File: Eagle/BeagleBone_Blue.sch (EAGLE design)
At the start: 129 parts, among them M1 JST_ZH_2, M2 JST_ZH_2, M3 JST_ZH_2, M4 JST_ZH_2, Q3 MOSFET-N

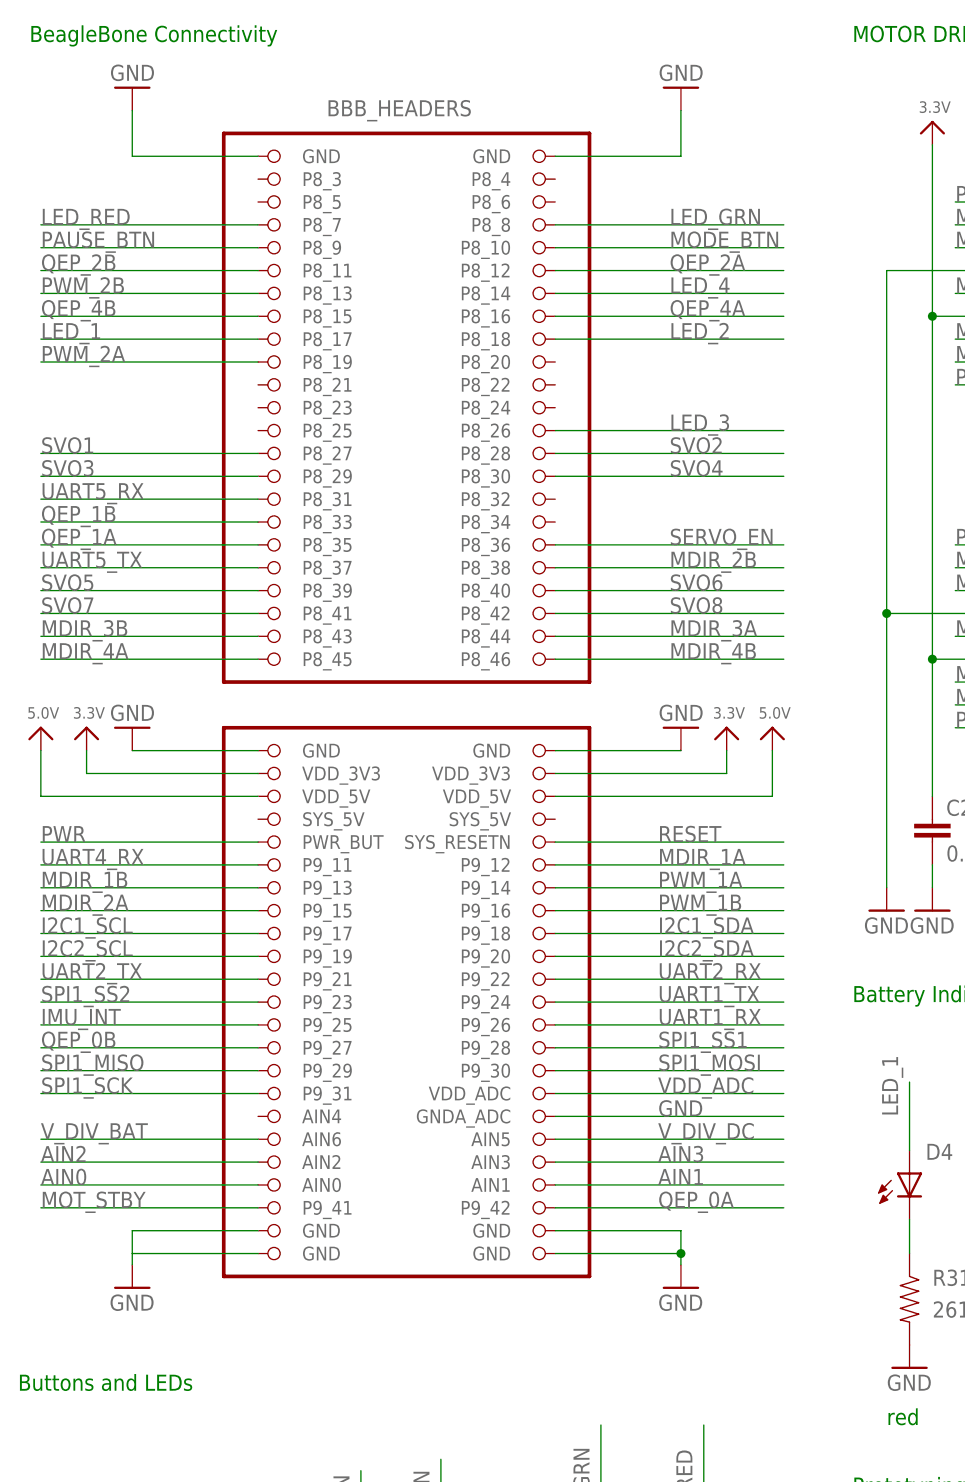
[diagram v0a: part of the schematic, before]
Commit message: Remove BeagleBone connectors
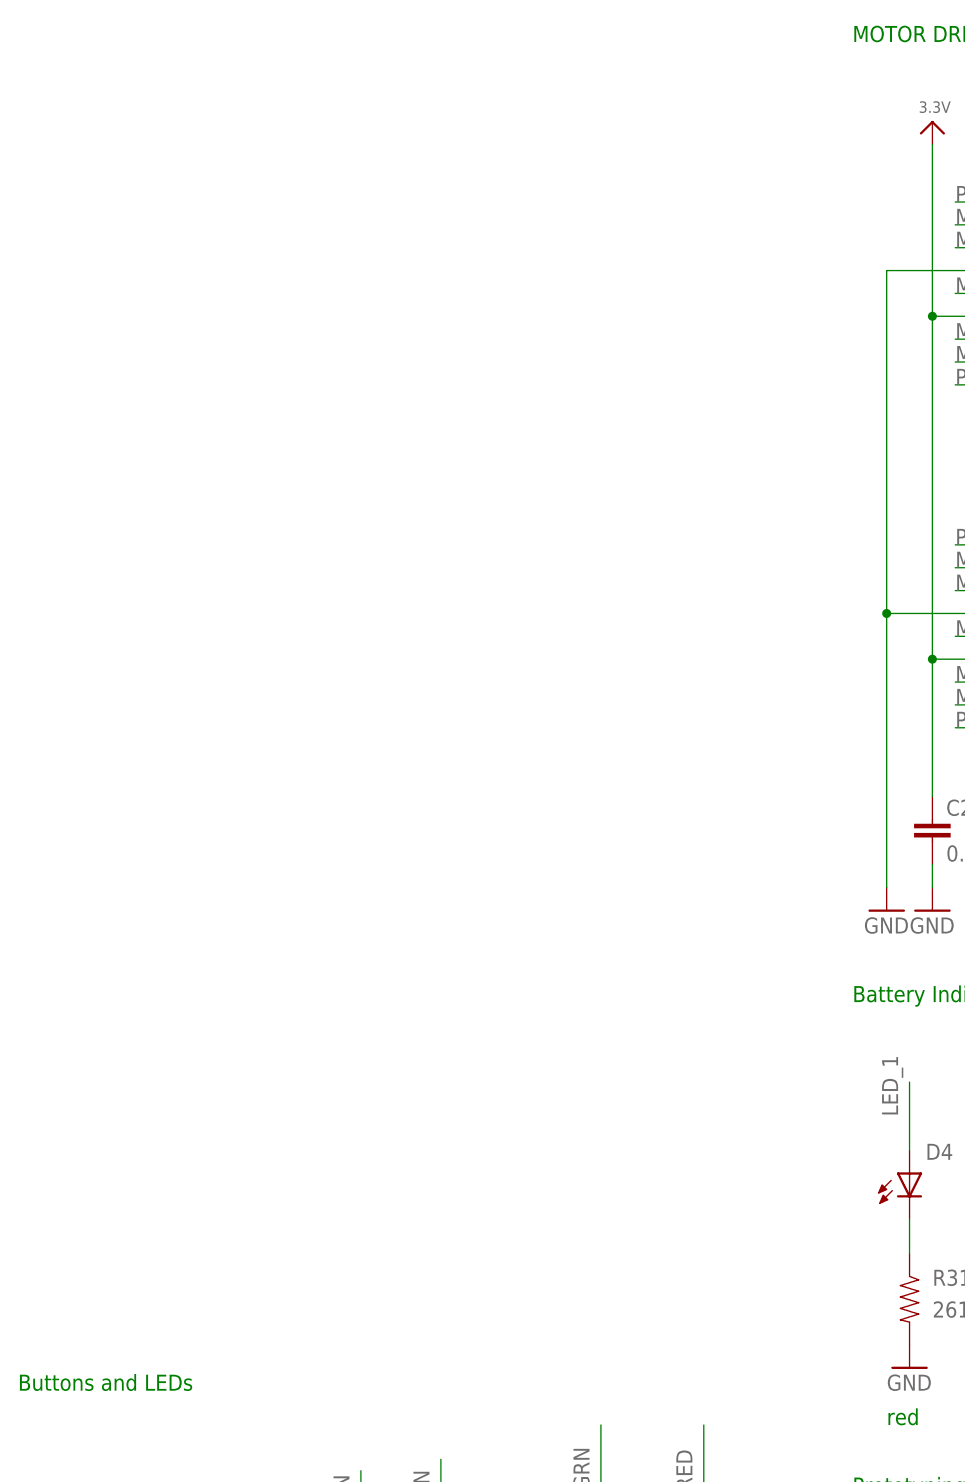
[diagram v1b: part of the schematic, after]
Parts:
- removed BBB_HEADERS: BEAGLEBONE_OUTLINE, Strawson_Eagle_Lib:BEAGLEBONE_OUTLINE
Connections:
- net 3.3V: no longer BBB_HEADERS.VDD_3V3@1, BBB_HEADERS.VDD_3V3@2
- net 5.0V: no longer BBB_HEADERS.VDD_5V@1, BBB_HEADERS.VDD_5V@2
- net AIN0: no longer BBB_HEADERS.AIN0
- net AIN1: no longer BBB_HEADERS.AIN1
- net AIN2: no longer BBB_HEADERS.AIN2
- net AIN3: no longer BBB_HEADERS.AIN3
- net GND: no longer BBB_HEADERS.GND@1, BBB_HEADERS.GND@2, BBB_HEADERS.GND@3, BBB_HEADERS.GND@4, BBB_HEADERS.GND@5, BBB_HEADERS.GND@6, BBB_HEADERS.GND@7, BBB_HEADERS.GND@8, BBB_HEADERS.GNDA_ADC
- net I2C1_SCL: no longer BBB_HEADERS.P9_17
- net I2C1_SDA: no longer BBB_HEADERS.P9_18
- net I2C2_SCL: no longer BBB_HEADERS.P9_19
- net I2C2_SDA: no longer BBB_HEADERS.P9_20
- net IMU_INT: no longer BBB_HEADERS.P9_25
- net LED_1: no longer BBB_HEADERS.P8_17
- net LED_2: no longer BBB_HEADERS.P8_18
- net LED_3: no longer BBB_HEADERS.P8_26
- net LED_4: no longer BBB_HEADERS.P8_14
- net LED_GRN: no longer BBB_HEADERS.P8_8
- net LED_RED: no longer BBB_HEADERS.P8_7
- net MDIR_1A: no longer BBB_HEADERS.P9_12
- net MDIR_1B: no longer BBB_HEADERS.P9_13
- net MDIR_2A: no longer BBB_HEADERS.P9_15
- net MDIR_2B: no longer BBB_HEADERS.P8_38
- net MDIR_3A: no longer BBB_HEADERS.P8_44
- net MDIR_3B: no longer BBB_HEADERS.P8_43
- net MDIR_4A: no longer BBB_HEADERS.P8_45
- net MDIR_4B: no longer BBB_HEADERS.P8_46
- net MODE_BTN: no longer BBB_HEADERS.P8_10
- net MOT_STBY: no longer BBB_HEADERS.P9_41
- net PAUSE_BTN: no longer BBB_HEADERS.P8_9
- net PWM_1A: no longer BBB_HEADERS.P9_14
- net PWM_1B: no longer BBB_HEADERS.P9_16
- net PWM_2A: no longer BBB_HEADERS.P8_19
- net PWM_2B: no longer BBB_HEADERS.P8_13
- net PWR: no longer BBB_HEADERS.PWR_BUT
- net QEP_0A: no longer BBB_HEADERS.P9_42
- net QEP_0B: no longer BBB_HEADERS.P9_27
- net QEP_1A: no longer BBB_HEADERS.P8_35
- net QEP_1B: no longer BBB_HEADERS.P8_33
- net QEP_2A: no longer BBB_HEADERS.P8_12
- net QEP_2B: no longer BBB_HEADERS.P8_11
- net QEP_4A: no longer BBB_HEADERS.P8_16
- net QEP_4B: no longer BBB_HEADERS.P8_15
- net RESET: no longer BBB_HEADERS.SYS_RESETN
- net SERVO_EN: no longer BBB_HEADERS.P8_36
- net SPI1_MISO: no longer BBB_HEADERS.P9_29
- net SPI1_MOSI: no longer BBB_HEADERS.P9_30
- net SPI1_SCK: no longer BBB_HEADERS.P9_31
- net SPI1_SS1: no longer BBB_HEADERS.P9_28
- net SPI1_SS2: no longer BBB_HEADERS.P9_23
- net SVO1: no longer BBB_HEADERS.P8_27
- net SVO2: no longer BBB_HEADERS.P8_28
- net SVO3: no longer BBB_HEADERS.P8_29
- net SVO4: no longer BBB_HEADERS.P8_30
- net SVO5: no longer BBB_HEADERS.P8_39
- net SVO6: no longer BBB_HEADERS.P8_40
- net SVO7: no longer BBB_HEADERS.P8_41
- net SVO8: no longer BBB_HEADERS.P8_42
- net UART1_RX: no longer BBB_HEADERS.P9_26
- net UART1_TX: no longer BBB_HEADERS.P9_24
- net UART2_RX: no longer BBB_HEADERS.P9_22
- net UART2_TX: no longer BBB_HEADERS.P9_21
- net UART4_RX: no longer BBB_HEADERS.P9_11
- net UART5_RX: no longer BBB_HEADERS.P8_31
- net UART5_TX: no longer BBB_HEADERS.P8_37
- net VDD_ADC: no longer BBB_HEADERS.VDD_ADC
- net V_DIV_BAT: no longer BBB_HEADERS.AIN6
- net V_DIV_DC: no longer BBB_HEADERS.AIN5
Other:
- note removed: "BeagleBone Connectivity"

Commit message: About to remove SIP1000
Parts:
- added IC1: (no value), GHI-SiP(Octavo):SIP1000
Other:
- note added: "BeagleBoard.org BeagleBone Blue Rev. -"
- note removed: "SD-101D"
- note removed: "Strawson Design Robotics Cape Rev. D"
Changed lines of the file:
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@@
 <part name="R8" library="Strawson_Eagle_Lib" deviceset="RESISTOR" device="0402-RES" value="10k"/>
 <part name="GND9" library="SparkFun-Aesthetics" deviceset="GND" device=""/>
+<part name="U$3" library="BeagleBone_Blue" deviceset="OSD3358" device=""/>
+<part name="U$4" library="BeagleBone_Blue" deviceset="OSD3358" device=""/>
+<part name="U$5" library="BeagleBone_Blue" deviceset="OSD3358" device=""/>
+<part name="U$7" library="BeagleBone_Blue" deviceset="OSD3358" device=""/>
+<part name="U$10" library="BeagleBone_Blue" deviceset="OSD3358" device=""/>
+<part name="U$11" library="BeagleBone_Blue" deviceset="OSD3358" device=""/>
+<part name="U$13" library="BeagleBone_Blue" deviceset="OSD3358" device=""/>
+<part name="U$14" library="BeagleBone_Blue" deviceset="OSD3358" device=""/>
+<part name="U$15" library="BeagleBone_Blue" deviceset="OSD3358" device=""/>
+<part name="U$16" library="BeagleBone_Blue" deviceset="OSD3358" device=""/>
+<part name="U$17" library="BeagleBone_Blue" deviceset="OSD3358" device=""/>
+<part name="U$18" library="BeagleBone_Blue" deviceset="OSD3358" device=""/>
+<part name="U$19" library="BeagleBone_Blue" deviceset="OSD3358" device=""/>
+<part name="U$20" library="BeagleBone_Blue" deviceset="OSD3358" device=""/>
+<part name="U$21" library="BeagleBone_Blue" deviceset="OSD3358" device=""/>
+<part name="U$22" library="BeagleBone_Blue" deviceset="OSD3358" device=""/>
+<part name="U$24" library="BeagleBone_Blue" deviceset="OSD3358" device=""/>
+<part name="U$25" library="BeagleBone_Blue" deviceset="OSD3358" device=""/>
+<part name="U$26" library="BeagleBone_Blue" deviceset="OSD3358" device=""/>
+<part name="U$27" library="BeagleBone_Blue" deviceset="OSD3358" device=""/>
+<part name="U$28" library="BeagleBone_Blue" deviceset="OSD3358" device=""/>
+<part name="U$29" library="BeagleBone_Blue" deviceset="OSD3358" device=""/>
+<part name="U$30" library="BeagleBone_Blue" deviceset="OSD3358" device=""/>
+<part name="IC1" library="GHI-SiP(Octavo)" deviceset="SIP1000" device=""/>
 </parts>
 <sheets>
 <sheet>
 <plain>
-<text x="290.83" y="8.89" size="3.556" layer="91" ratio="10">Strawson Design
-Robotics Cape
-Rev. D</text>
+<text x="290.83" y="8.89" size="3.556" layer="91" ratio="10">BeagleBoard.org
+BeagleBone Blue
+Rev. -</text>
 <text x="356.87" y="140.97" size="1.778" layer="91">Barrel Connector
 Center Positive
@@
 <text x="99.06" y="55.88" size="1.778" layer="91" rot="MR0" align="top-right">ADC Dividers</text>
 <text x="99.06" y="91.44" size="1.778" layer="91">Prototyping Power Rails</text>
-<text x="344.17" y="19.685" size="3.556" layer="91" ratio="10">SD-101D</text>
+<text x="344.17" y="19.685" size="3.556" layer="91" ratio="10"></text>
 <text x="6.35" y="102.87" size="1.778" layer="91">Buttons and LEDs</text>
 <text x="228.6" y="146.05" size="1.778" layer="91">eQEP Encoder Plugs JST SH</text>
@@
 </nets>
 </sheet>
+<sheet>
+<plain>
+<frame x1="0" y1="0" x2="381" y2="271.78" columns="8" rows="5" layer="91"/>
+</plain>
+<instances>
+<instance part="IC1" gate="A" x="50.8" y="198.12"/>
+<instance part="IC1" gate="B" x="182.88" y="182.88"/>
+<instance part="IC1" gate="C" x="307.34" y="193.04"/>
+<instance part="IC1" gate="E" x="68.58" y="73.66"/>
+<instance part="IC1" gate="F" x="254" y="58.42"/>
+</instances>
+<busses>
+</busses>
+<nets>
+</nets>
+</sheet>

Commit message: Removed old part
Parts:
- removed IC1: (no value), GHI-SiP(Octavo):SIP1000
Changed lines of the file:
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@@
 <part name="U$29" library="BeagleBone_Blue" deviceset="OSD3358" device=""/>
 <part name="U$30" library="BeagleBone_Blue" deviceset="OSD3358" device=""/>
-<part name="IC1" library="GHI-SiP(Octavo)" deviceset="SIP1000" device=""/>
 </parts>
 <sheets>
@@
 </plain>
 <instances>
-<instance part="IC1" gate="A" x="50.8" y="198.12"/>
-<instance part="IC1" gate="B" x="182.88" y="182.88"/>
-<instance part="IC1" gate="C" x="307.34" y="193.04"/>
-<instance part="IC1" gate="E" x="68.58" y="73.66"/>
-<instance part="IC1" gate="F" x="254" y="58.42"/>
 </instances>
 <busses>

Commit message: Placed SIP and connected power
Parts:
- added U$10, U$11, U$13, U$14, U$15, U$16, U$17, U$18, U$19, U$20, U$21, U$22, U$24, U$25, U$26, U$27, U$28, U$29, U$3, U$30, U$4, U$5, U$7, U1: OSD3358, BeagleBone_Blue:OSD3358
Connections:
- net 5.0V: now also U1A.VIN_AC_0, U1A.VIN_AC_1
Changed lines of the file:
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@@
 <part name="U$29" library="BeagleBone_Blue" deviceset="OSD3358" device=""/>
 <part name="U$30" library="BeagleBone_Blue" deviceset="OSD3358" device=""/>
+<part name="U1" library="BeagleBone_Blue" deviceset="OSD3358" device=""/>
 </parts>
 <sheets>
@@
 </plain>
 <instances>
+<instance part="U1" gate="B" x="246.38" y="78.74"/>
+<instance part="U1" gate="A" x="71.12" y="187.96"/>
+<instance part="U1" gate="C" x="71.12" y="33.02"/>
 </instances>
 <busses>
+</busses>
+<nets>
+<net name="5.0V" class="0">
+<segment>
+<pinref part="U1" gate="A" pin="VIN_AC_0"/>
+<wire x1="66.04" y1="248.92" x2="53.34" y2="248.92" width="0.1524" layer="91"/>
+<wire x1="53.34" y1="248.92" x2="53.34" y2="246.38" width="0.1524" layer="91"/>
+<pinref part="U1" gate="A" pin="VIN_AC_1"/>
+<wire x1="53.34" y1="246.38" x2="66.04" y2="246.38" width="0.1524" layer="91"/>
+<wire x1="53.34" y1="248.92" x2="43.18" y2="248.92" width="0.1524" layer="91"/>
+<junction x="53.34" y="248.92"/>
+<label x="43.18" y="248.92" size="1.778" layer="95"/>
+</segment>
+</net>
+</nets>
+</sheet>
+<sheet>
+<plain>
+<frame x1="124.46" y1="-60.96" x2="436.88" y2="142.24" columns="8" rows="5" layer="91"/>
+</plain>
+<instances>
+<instance part="U1" gate="E" x="210.82" y="48.26"/>
+<instance part="U1" gate="F" x="345.44" y="48.26"/>
+</instances>
+<busses>
